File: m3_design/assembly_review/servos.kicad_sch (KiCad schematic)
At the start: 12 parts, among them J122 SERVO 3x4

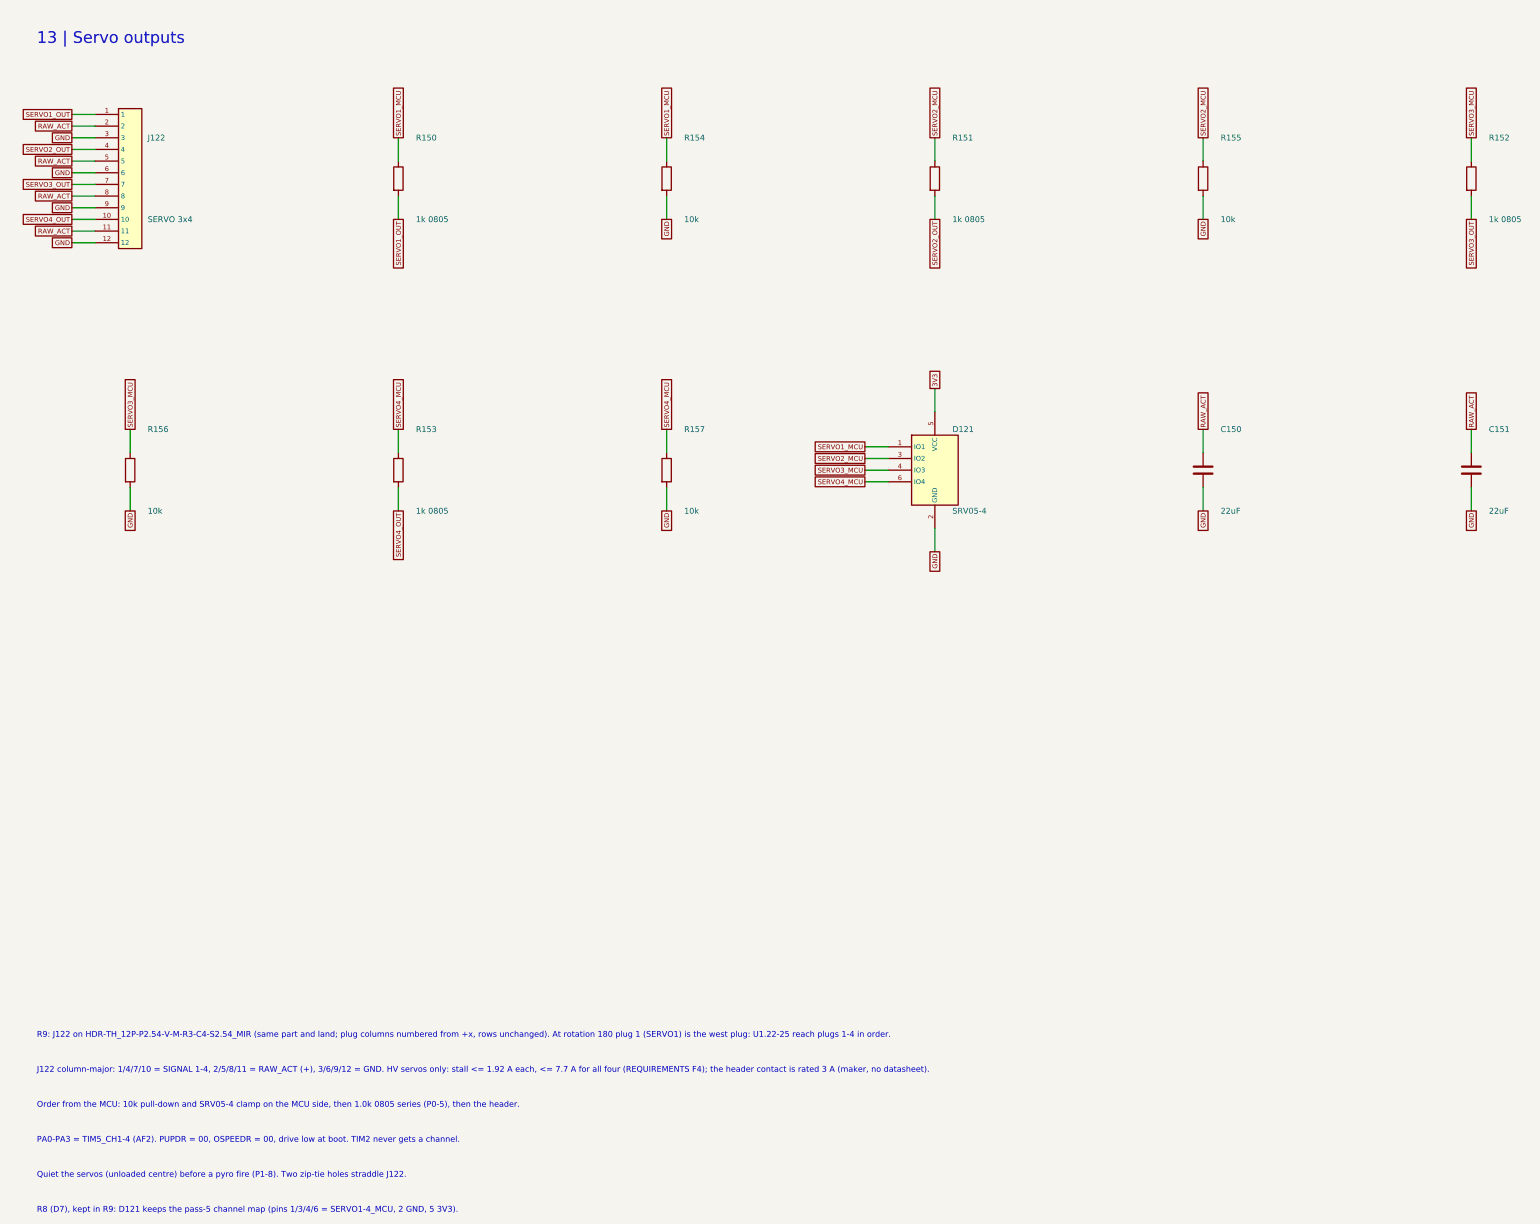
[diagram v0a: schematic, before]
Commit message: R10: m3_design/r10_build.sh and per-family stage gate; m3_design/assembly_review rebuilt as M3-ASSY-R10 (board 883d2db5..., 46 x 90 mm); tools/check.sh passes at zero; binding note bound to the board
Co-Authored-By: Claude Opus 5.5 <noreply@anthropic.com>
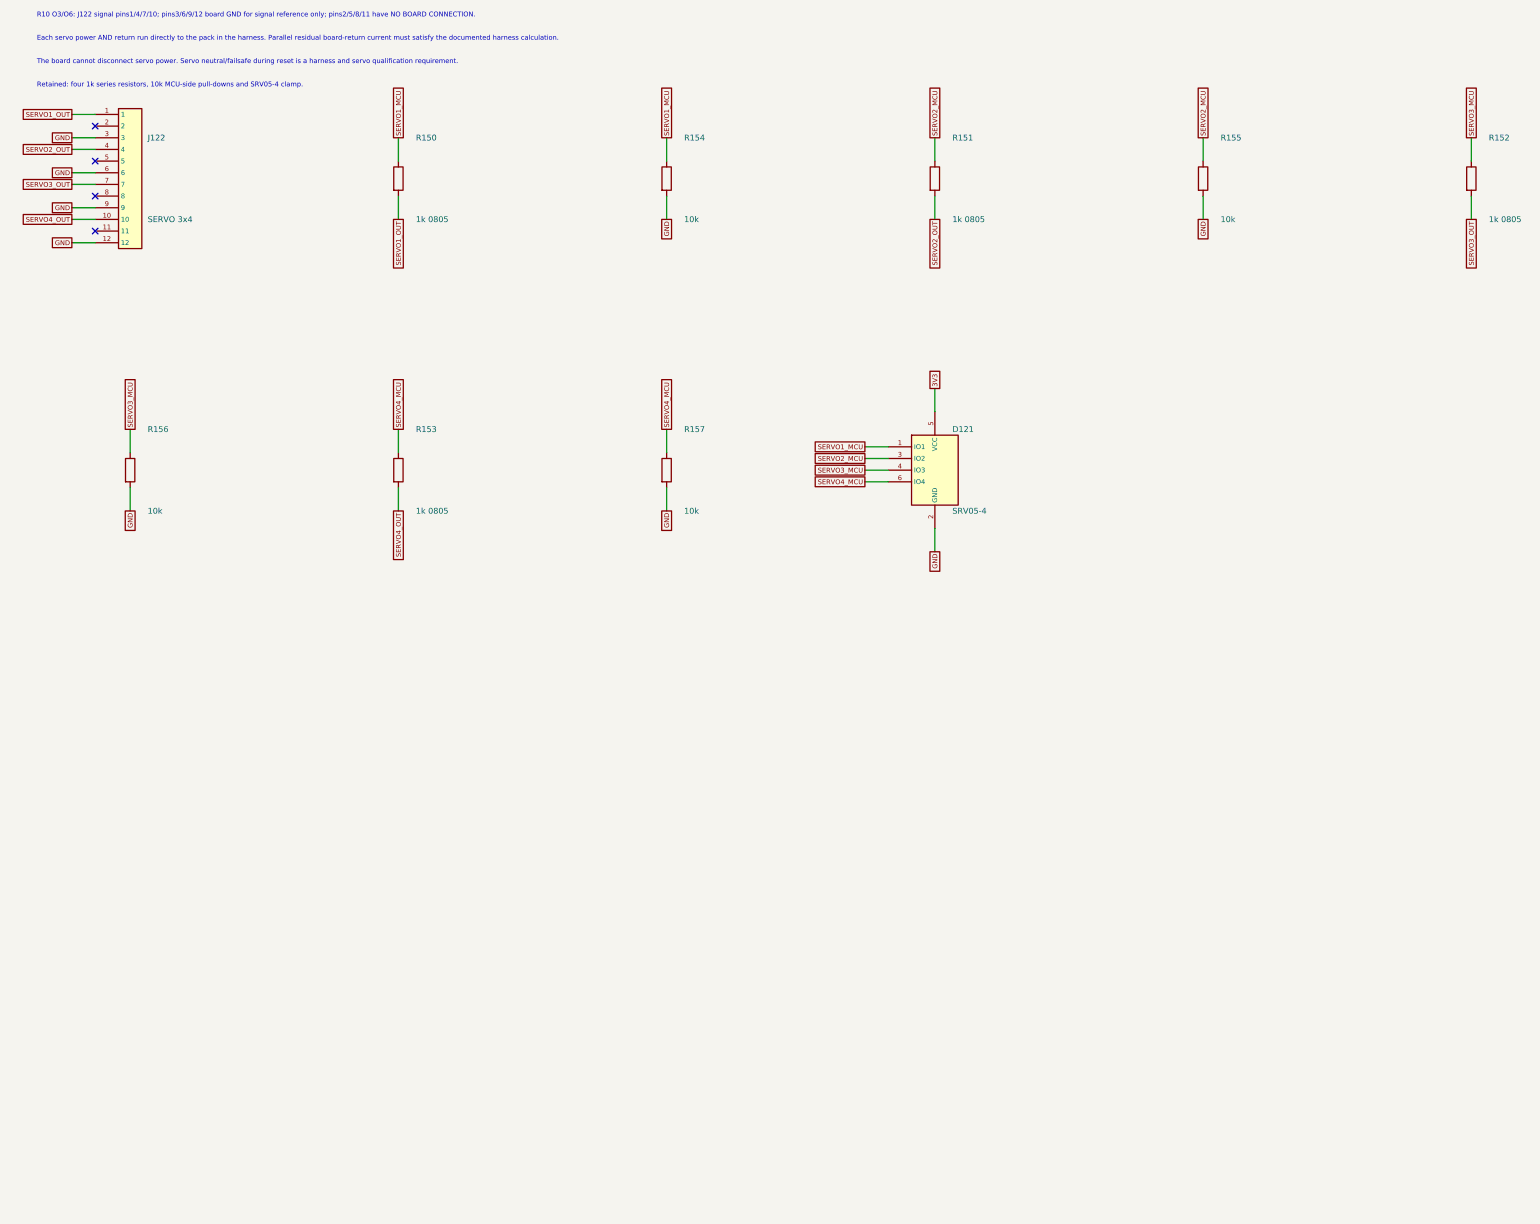
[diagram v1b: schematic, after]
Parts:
- removed C150, C151: 22uF, rocket:C0805, symbol M3:C
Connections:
- removed net RAW_ACT: J122.11, J122.2, J122.5, J122.8
- no-connect marks 0 -> 4
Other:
- note added: "Each servo power AND return run directly to the pack in the harness. Parallel residual board-return current must satisfy the documented harness calculation."
- note added: "R10 O3/O6: J122 signal pins1/4/7/10; pins3/6/9/12 board GND for signal reference only; pins2/5/8/11 have NO BOARD CONNECTION."
- note added: "Retained: four 1k series resistors, 10k MCU-side pull-downs and SRV05-4 clamp."
- note added: "The board cannot disconnect servo power. Servo neutral/failsafe during reset is a harness and servo qualification requirement."
- note removed: "13 | Servo outputs"
- note removed: "J122 column-major: 1/4/7/10 = SIGNAL 1-4, 2/5/8/11 = RAW_ACT (+), 3/6/9/12 = GND. HV servos only: stall <= 1.92 A each, <= 7.7 A for all four (REQUIREMENTS F4); the header contact is rated 3 A (maker, no datasheet)."
- note removed: "Order from the MCU: 10k pull-down and SRV05-4 clamp on the MCU side, then 1.0k 0805 series (P0-5), then the header."
- note removed: "PA0-PA3 = TIM5_CH1-4 (AF2). PUPDR = 00, OSPEEDR = 00, drive low at boot. TIM2 never gets a channel."
- note removed: "Quiet the servos (unloaded centre) before a pyro fire (P1-8). Two zip-tie holes straddle J122."
- note removed: "R8 (D7), kept in R9: D121 keeps the pass-5 channel map (pins 1/3/4/6 = SERVO1-4_MCU, 2 GND, 5 3V3)."
- note removed: "R9: J122 on HDR-TH_12P-P2.54-V-M-R3-C4-S2.54_MIR (same part and land; plug columns numbered from +x, rows unchanged). At rotation 180 plug 1 (SERVO1) is the west plug: U1.22-25 reach plugs 1-4 in order."

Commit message: R10 requirements-audit cuts and GAP fixes before review round 9
Implement adopted AUD-1 through AUD-10 and GAP-1 through GAP-5 after the single-switch pass.
Remove the advisory pull-pin, redundant probes and GPS/radio IO LDO cells; qualify the smaller
AONR21357 pair, correct C120 voltage rating, standardize shared-code capacitor lands, simplify
slow returns and fire-only copper, localize U9 output protection and add exactly two U401 VIPPO vias.
Record physical-current timing, coupled fire/source budget, C84 manual fitting and narrowed gate scopes.

Board SHA-256: 877d01996a59e9dd5c6dbc367274bb9a323a13982d67960fe46df9b0ee53205d
Board: 46 x 90 mm, 4 layers, 2365477 bytes; 225 footprints, 883 straight tracks, 323 vias.
Netlist SHA-256: 0843da709e2d7a757e9b35cdff48158a54012c5353619cbf409ab961efd2c3ca
Two fresh complete passing builds are byte-identical. Schematic: 700 pins; 22 seeded faults detected.

Final unskipped tools/check.sh: exit 0
DRC violations 0  unconnected 0  schematic parity 0  ERC 0
metadata / 3D model audit: OK
silkscreen outside the board outline: 0 stroke points
fit check: OK (CAD envelopes only)
R10 CAD contract (full): OK
routing hygiene: 0 failing, 0 allowlisted, 0 leftovers recorded
actuator safety contract: OK
Fab manifest: OK; 5 outputs match current CAD and export inputs
Self-tests: shell 4, fit 24, paste 5, routing 59, R10 131; three NumPy cases rerun and passed.

Fab: 215 CPL rows, 82 BOM codes; orientation / paste / manifest pass. Hot-plug: 2304 required
cases plus convergence and controls pass (simulation / Inference). Plate f1 280.9 Hz (Inference).
Live JLC: $84.43 vs $84.41 target, 46 Extended codes; R430 / U4 short. Procurement exit 1 is a
disclosed OQ-3 / ordering deviation, not a CAD gate pass. No quote accepted or order placed.
Firmware, bench, thermal/transient correlation, process acceptance, installed RF immunity and physical fit unverified.

This preparatory pass earns no clean-review credit. Start fresh full ten-lens round 9 on th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
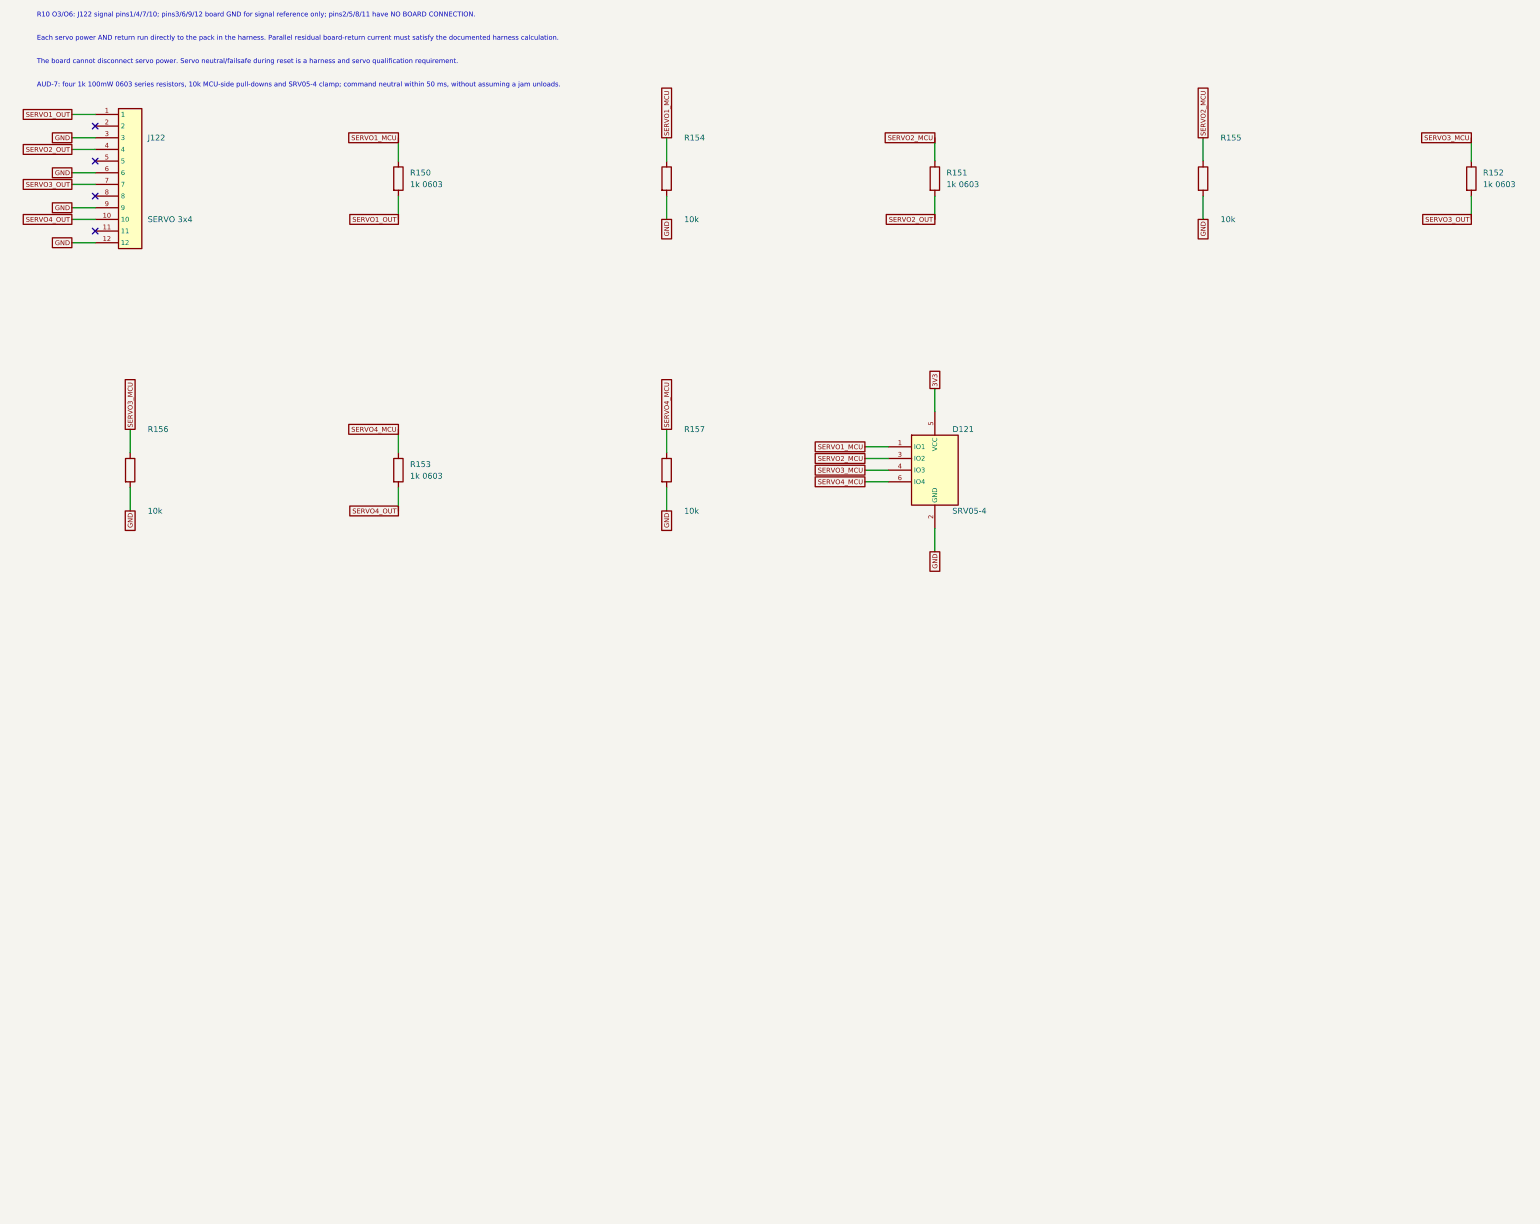
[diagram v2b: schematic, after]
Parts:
- R150, R151, R152, R153: value 1k 0805 -> 1k 0603; footprint rocket:R0805 -> rocket:R_0603_1608Metric; LCSC C17513 -> C21190; Manufacturer Part 0805W8F1001T5E -> 0603WAF1001T5E
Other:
- note added: "AUD-7: four 1k 100mW 0603 series resistors, 10k MCU-side pull-downs and SRV05-4 clamp; command neutral within 50 ms, without assuming a jam unloads."
- note removed: "Retained: four 1k series resistors, 10k MCU-side pull-downs and SRV05-4 clamp."
